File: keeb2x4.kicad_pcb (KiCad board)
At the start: 2 copper layers, 100.6 x 39.9 mm, 36 parts, among them J1 USB_mini_micro_B, K1 KEYSW, K2 KEYSW, K3 KEYSW, K4 KEYSW, K5 KEYSW, K6 KEYSW, K7 KEYSW, K8 KEYSW, SW1 SW_PUSH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

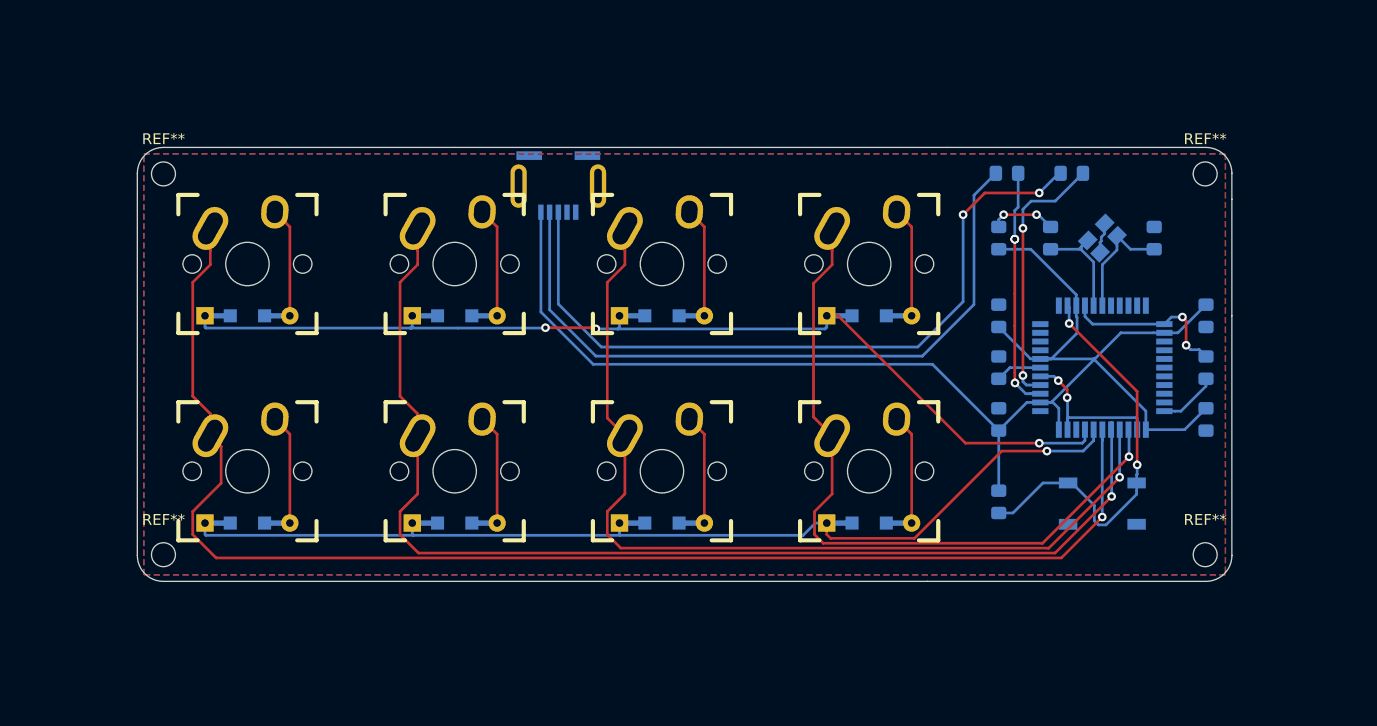
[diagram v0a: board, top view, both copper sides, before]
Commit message: Updated pcb dimensions
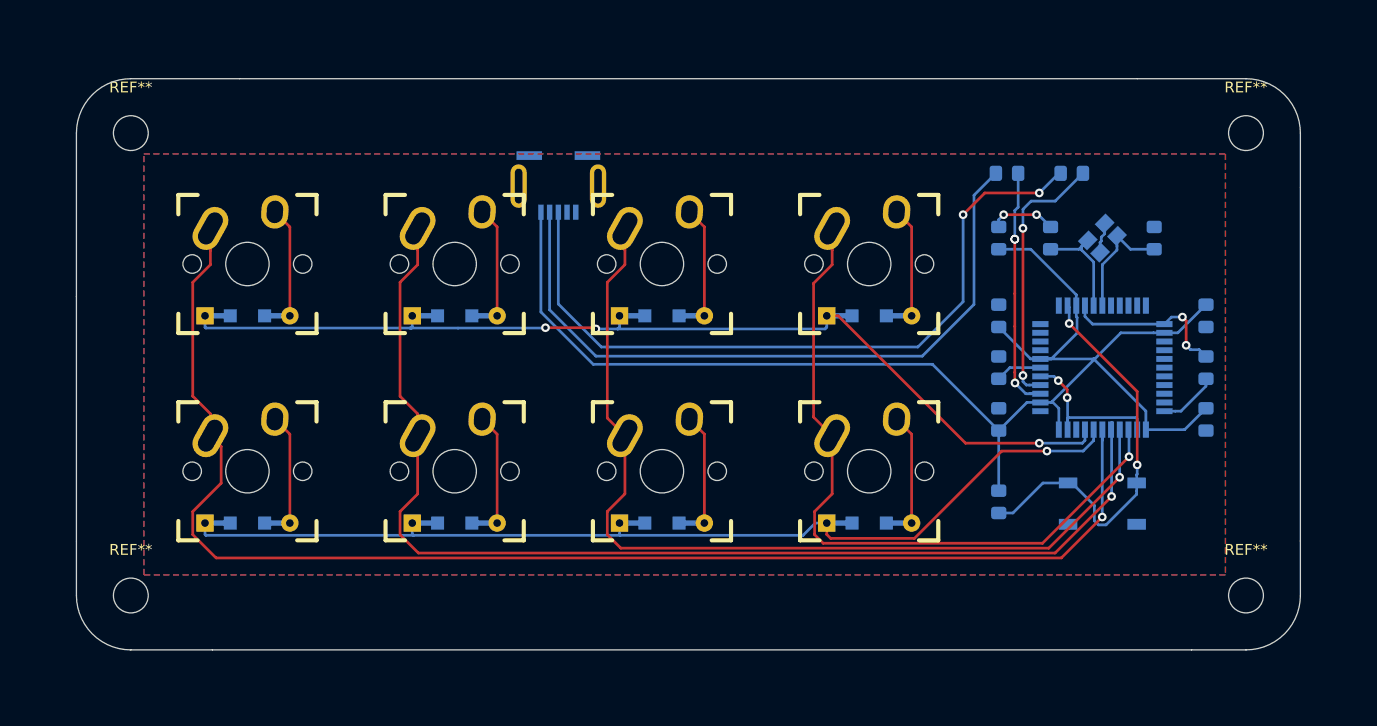
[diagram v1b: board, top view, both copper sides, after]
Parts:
- removed the REF** at (28.0, 86.2)
- removed the REF** at (123.8, 86.2)
- removed the REF** at (123.8, 51.2)
- removed the REF** at (28.0, 51.2)
- added REF**: M3_4, MountingHole:MountingHole_3.2mm_M3, F.Cu at (127.5, 90.0)
- added REF**: M3_3, MountingHole:MountingHole_3.2mm_M3, F.Cu at (25.0, 90.0)
- added REF**: M3_2, MountingHole:MountingHole_3.2mm_M3, F.Cu at (127.5, 47.5)
- added REF**: M3_1, MountingHole:MountingHole_3.2mm_M3, F.Cu at (25.0, 47.5)
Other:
- board size 100.6 x 39.9 mm -> 112.5 x 52.5 mm
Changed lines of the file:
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@@
   (general
     (thickness 1.6)
-    (drawings 14)
+    (drawings 16)
     (tracks 279)
     (zones 0)
@@
     (add_net VCC)
   )
-  (module MountingHole:MountingHole_2.2mm_M2 (layer F.Cu)
-    (at 28 86.25)
-    (descr "Mounting Hole 2.2mm, no annular, M2")
-    (tags "mounting hole 2.2mm no annular m2")
+  (module MountingHole:MountingHole_3.2mm_M3 (layer F.Cu)
+    (at 127.5 90)
+    (descr "Mounting Hole 3.2mm, no annular, M3")
+    (tags "mounting hole 3.2mm no annular m3")
     (attr virtual)
-    (fp_text reference REF** (at 0 -3.2) (layer F.SilkS)
+    (fp_text reference REF** (at 0 -4.2) (layer F.SilkS)
       (effects (font (size 1 1) (thickness 0.15)))
     )
-    (fp_text value M3 (at 0 3.2) (layer F.Fab)
+    (fp_text value M3_4 (at 0 4.2) (layer F.Fab)
       (effects (font (size 1 1) (thickness 0.15)))
     )
-    (fp_circle (center 0 0) (end 2.45 0) (layer F.CrtYd) (width 0.05))
-    (fp_circle (center 0 0) (end 2.2 0) (layer Cmts.User) (width 0.15))
+    (fp_circle (center 0 0) (end 3.45 0) (layer F.CrtYd) (width 0.05))
+    (fp_circle (center 0 0) (end 3.2 0) (layer Cmts.User) (width 0.15))
     (fp_text user %R (at 0.3 0) (layer F.Fab)
       (effects (font (size 1 1) (thickness 0.15)))
     )
-    (pad 1 np_thru_hole circle (at 0 0) (size 2.2 2.2) (drill 2.2) (layers *.Cu *.Mask))
-  )
-  (module MountingHole:MountingHole_2.2mm_M2 (layer F.Cu)
-    (at 123.75 86.25)
-    (descr "Mounting Hole 2.2mm, no annular, M2")
-    (tags "mounting hole 2.2mm no annular m2")
+    (pad 1 np_thru_hole circle (at 0 0) (size 3.2 3.2) (drill 3.2) (layers *.Cu *.Mask))
+  )
+  (module MountingHole:MountingHole_3.2mm_M3 (layer F.Cu)
+    (at 25 90)
+    (descr "Mounting Hole 3.2mm, no annular, M3")
+    (tags "mounting hole 3.2mm no annular m3")
     (attr virtual)
-    (fp_text reference REF** (at 0 -3.2) (layer F.SilkS)
+    (fp_text reference REF** (at 0 -4.2) (layer F.SilkS)
       (effects (font (size 1 1) (thickness 0.15)))
     )
-    (fp_text value M4 (at 0 3.2) (layer F.Fab)
+    (fp_text value M3_3 (at 0 4.2) (layer F.Fab)
       (effects (font (size 1 1) (thickness 0.15)))
     )
-    (fp_circle (center 0 0) (end 2.45 0) (layer F.CrtYd) (width 0.05))
-    (fp_circle (center 0 0) (end 2.2 0) (layer Cmts.User) (width 0.15))
+    (fp_circle (center 0 0) (end 3.45 0) (layer F.CrtYd) (width 0.05))
+    (fp_circle (center 0 0) (end 3.2 0) (layer Cmts.User) (width 0.15))
     (fp_text user %R (at 0.3 0) (layer F.Fab)
       (effects (font (size 1 1) (thickness 0.15)))
     )
-    (pad 1 np_thru_hole circle (at 0 0) (size 2.2 2.2) (drill 2.2) (layers *.Cu *.Mask))
-  )
-  (module MountingHole:MountingHole_2.2mm_M2 (layer F.Cu)
-    (at 123.75 51.25)
-    (descr "Mounting Hole 2.2mm, no annular, M2")
-    (tags "mounting hole 2.2mm no annular m2")
+    (pad 1 np_thru_hole circle (at 0 0) (size 3.2 3.2) (drill 3.2) (layers *.Cu *.Mask))
+  )
+  (module MountingHole:MountingHole_3.2mm_M3 (layer F.Cu)
+    (at 127.5 47.5)
+    (descr "Mounting Hole 3.2mm, no annular, M3")
+    (tags "mounting hole 3.2mm no annular m3")
     (attr virtual)
-    (fp_text reference REF** (at 0 -3.2) (layer F.SilkS)
+    (fp_text reference REF** (at 0 -4.2) (layer F.SilkS)
       (effects (font (size 1 1) (thickness 0.15)))
     )
-    (fp_text value M2 (at 0 3.2) (layer F.Fab)
+    (fp_text value M3_2 (at 0 4.2) (layer F.Fab)
       (effects (font (size 1 1) (thickness 0.15)))
     )
-    (fp_circle (center 0 0) (end 2.45 0) (layer F.CrtYd) (width 0.05))
-    (fp_circle (center 0 0) (end 2.2 0) (layer Cmts.User) (width 0.15))
+    (fp_circle (center 0 0) (end 3.45 0) (layer F.CrtYd) (width 0.05))
+    (fp_circle (center 0 0) (end 3.2 0) (layer Cmts.User) (width 0.15))
     (fp_text user %R (at 0.3 0) (layer F.Fab)
       (effects (font (size 1 1) (thickness 0.15)))
     )
-    (pad 1 np_thru_hole circle (at 0 0) (size 2.2 2.2) (drill 2.2) (layers *.Cu *.Mask))
-  )
-  (module MountingHole:MountingHole_2.2mm_M2 (layer F.Cu)
-    (at 28 51.25)
-    (descr "Mounting Hole 2.2mm, no annular, M2")
-    (tags "mounting hole 2.2mm no annular m2")
+    (pad 1 np_thru_hole circle (at 0 0) (size 3.2 3.2) (drill 3.2) (layers *.Cu *.Mask))
+  )
+  (module MountingHole:MountingHole_3.2mm_M3 (layer F.Cu)
+    (at 25 47.5)
+    (descr "Mounting Hole 3.2mm, no annular, M3")
+    (tags "mounting hole 3.2mm no annular m3")
     (attr virtual)
-    (fp_text reference REF** (at 0 -3.2) (layer F.SilkS)
+    (fp_text reference REF** (at 0 -4.2) (layer F.SilkS)
       (effects (font (size 1 1) (thickness 0.15)))
     )
-    (fp_text value M1 (at 0 3.2) (layer F.Fab)
+    (fp_text value M3_1 (at 0 4.2) (layer F.Fab)
       (effects (font (size 1 1) (thickness 0.15)))
     )
-    (fp_circle (center 0 0) (end 2.45 0) (layer F.CrtYd) (width 0.05))
-    (fp_circle (center 0 0) (end 2.2 0) (layer Cmts.User) (width 0.15))
+    (fp_circle (center 0 0) (end 3.45 0) (layer F.CrtYd) (width 0.05))
+    (fp_circle (center 0 0) (end 3.2 0) (layer Cmts.User) (width 0.15))
     (fp_text user %R (at 0.3 0) (layer F.Fab)
       (effects (font (size 1 1) (thickness 0.15)))
     )
-    (pad 1 np_thru_hole circle (at 0 0) (size 2.2 2.2) (drill 2.2) (layers *.Cu *.Mask))
+    (pad 1 np_thru_hole circle (at 0 0) (size 3.2 3.2) (drill 3.2) (layers *.Cu *.Mask))
   )
   (module Capacitor_SMD:C_0805_2012Metric_Pad1.15x1.40mm_HandSolder (layer B.Cu)
@@
     )
   )
-  (gr_line (start 27.979711 88.701637) (end 98.226645 88.701637) (layer Edge.Cuts) (width 0.05))
-  (gr_arc (start 27.979711 86.320385) (end 25.598459 86.320385) (angle -90) (layer Edge.Cuts) (width 0.05))
-  (gr_line (start 123.825104 88.701637) (end 98.226645 88.701637) (layer Edge.Cuts) (width 0.05))
-  (gr_line (start 27.979711 48.815666) (end 54.768796 48.815666) (layer Edge.Cuts) (width 0.05))
-  (gr_line (start 25.598459 86.320385) (end 25.598459 51.196918) (layer Edge.Cuts) (width 0.05))
-  (gr_arc (start 27.979711 51.196918) (end 27.979711 48.815666) (angle -90) (layer Edge.Cuts) (width 0.05))
-  (gr_arc (start 123.825104 86.320385) (end 123.825104 88.701637) (angle -90) (layer Edge.Cuts) (width 0.05))
-  (gr_line (start 126.206356 64.293804) (end 126.206356 86.320385) (layer Edge.Cuts) (width 0.05))
-  (gr_line (start 123.825104 48.815666) (end 119.0626 48.815666) (layer Edge.Cuts) (width 0.05))
-  (gr_line (start 126.206356 53.57817) (end 126.206356 51.196918) (layer Edge.Cuts) (width 0.05))
-  (gr_arc (start 123.825104 51.196918) (end 126.206356 51.196918) (angle -90) (layer Edge.Cuts) (width 0.05))
-  (gr_line (start 126.206356 64.293804) (end 126.206356 53.57817) (layer Edge.Cuts) (width 0.05))
-  (gr_line (start 100.012584 48.815666) (end 119.0626 48.815666) (layer Edge.Cuts) (width 0.05))
-  (gr_line (start 54.768796 48.815666) (end 100.012584 48.815666) (layer Edge.Cuts) (width 0.05))
+  (gr_line (start 132.5 47.5) (end 132.5 52.5) (layer Edge.Cuts) (width 0.05))
+  (gr_line (start 117.5 42.5) (end 127.5 42.5) (layer Edge.Cuts) (width 0.05))
+  (gr_line (start 25 42.5) (end 35 42.5) (layer Edge.Cuts) (width 0.05))
+  (gr_line (start 20 62.5) (end 20 47.5) (layer Edge.Cuts) (width 0.05))
+  (gr_line (start 20 90) (end 20 85) (layer Edge.Cuts) (width 0.05))
+  (gr_line (start 32.5 95) (end 25 95) (layer Edge.Cuts) (width 0.05))
+  (gr_line (start 127.5 95) (end 122.5 95) (layer Edge.Cuts) (width 0.05))
+  (gr_line (start 132.5 90) (end 132.5 85) (layer Edge.Cuts) (width 0.05))
+  (gr_arc (start 127.5 90) (end 127.5 95) (angle -90) (layer Edge.Cuts) (width 0.05))
+  (gr_arc (start 127.5 47.5) (end 132.5 47.5) (angle -90) (layer Edge.Cuts) (width 0.05))
+  (gr_arc (start 25 47.5) (end 25 42.5) (angle -90) (layer Edge.Cuts) (width 0.05))
+  (gr_arc (start 25 90) (end 20 90) (angle -90) (layer Edge.Cuts) (width 0.05))
+  (gr_line (start 20 62.5) (end 20 85) (layer Edge.Cuts) (width 0.05))
+  (gr_line (start 132.5 52.5) (end 132.5 85) (layer Edge.Cuts) (width 0.05))
+  (gr_line (start 35 42.5) (end 117.5 42.5) (layer Edge.Cuts) (width 0.05))
+  (gr_line (start 32.5 95) (end 122.5 95) (layer Edge.Cuts) (width 0.05))
   (segment (start 114.200746 57.066411) (end 114.512132 56.755025) (width 0.25) (layer B.Cu) (net 1))
   (segment (start 114.512132 56.755025) (end 114.512132 55.806497) (width 0.25) (layer B.Cu) (net 1))

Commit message: added case files
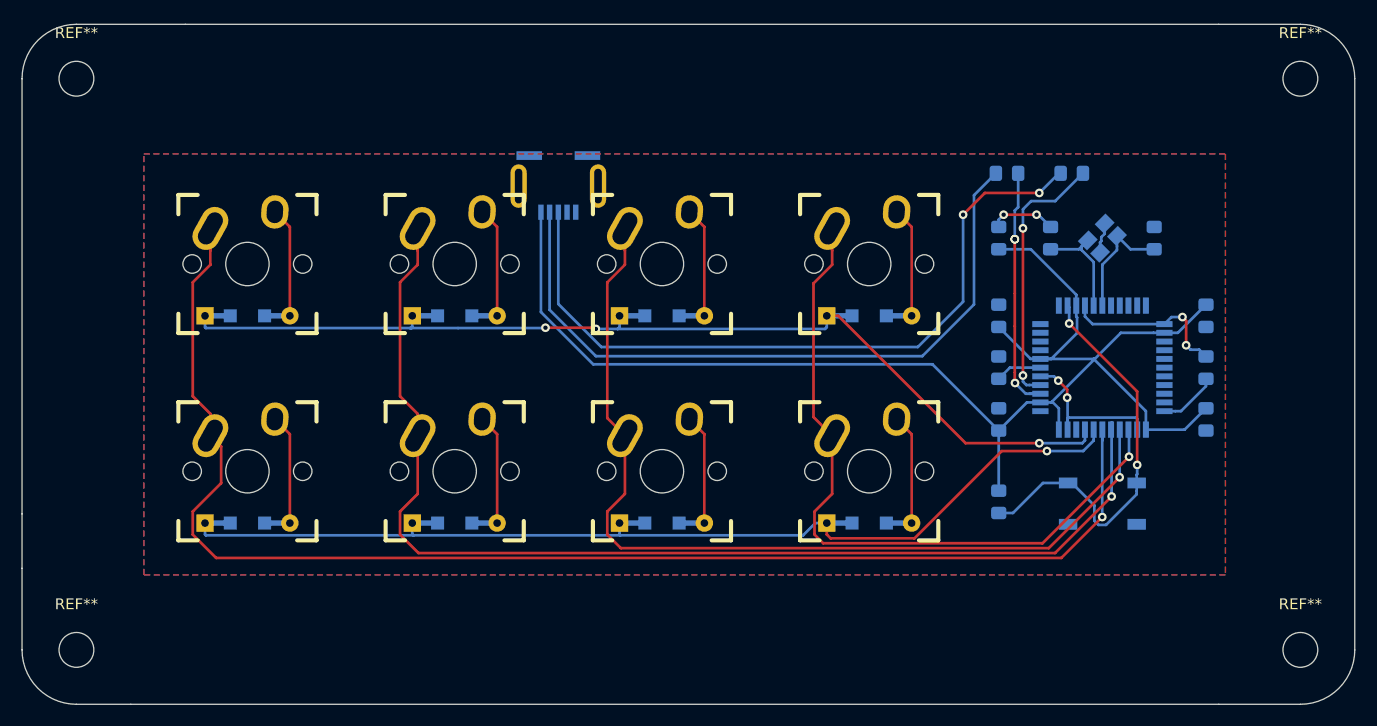
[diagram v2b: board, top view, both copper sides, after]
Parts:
- moved REF** 7.07 mm to (132.5, 95.0)
- moved REF** 7.07 mm to (20.0, 95.0)
- moved REF** 7.07 mm to (132.5, 42.5)
- moved REF** 7.07 mm to (20.0, 42.5)
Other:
- board size 112.5 x 52.5 mm -> 122.5 x 62.5 mm
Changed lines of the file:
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@@
   (general
     (thickness 1.6)
-    (drawings 16)
+    (drawings 14)
     (tracks 279)
     (zones 0)
@@
     (pcbplotparams
       (layerselection 0x010fc_ffffffff)
-      (usegerberextensions false)
+      (usegerberextensions true)
       (usegerberattributes false)
       (usegerberadvancedattributes false)
@@
       (outputformat 1)
       (mirror false)
-      (drillshape 1)
+      (drillshape 0)
       (scaleselection 1)
-      (outputdirectory ""))
+      (outputdirectory "gerber/"))
   )
   (net 0 "")
@@
   )
   (module MountingHole:MountingHole_3.2mm_M3 (layer F.Cu)
-    (at 127.5 90)
+    (at 132.5 95)
     (descr "Mounting Hole 3.2mm, no annular, M3")
     (tags "mounting hole 3.2mm no annular m3")
@@
   )
   (module MountingHole:MountingHole_3.2mm_M3 (layer F.Cu)
-    (at 25 90)
+    (at 20 95)
     (descr "Mounting Hole 3.2mm, no annular, M3")
     (tags "mounting hole 3.2mm no annular m3")
@@
   )
   (module MountingHole:MountingHole_3.2mm_M3 (layer F.Cu)
-    (at 127.5 47.5)
+    (at 132.5 42.5)
     (descr "Mounting Hole 3.2mm, no annular, M3")
     (tags "mounting hole 3.2mm no annular m3")
@@
   )
   (module MountingHole:MountingHole_3.2mm_M3 (layer F.Cu)
-    (at 25 47.5)
+    (at 20 42.5)
     (descr "Mounting Hole 3.2mm, no annular, M3")
     (tags "mounting hole 3.2mm no annular m3")
@@
     )
   )
-  (gr_line (start 132.5 47.5) (end 132.5 52.5) (layer Edge.Cuts) (width 0.05))
-  (gr_line (start 117.5 42.5) (end 127.5 42.5) (layer Edge.Cuts) (width 0.05))
-  (gr_line (start 25 42.5) (end 35 42.5) (layer Edge.Cuts) (width 0.05))
-  (gr_line (start 20 62.5) (end 20 47.5) (layer Edge.Cuts) (width 0.05))
-  (gr_line (start 20 90) (end 20 85) (layer Edge.Cuts) (width 0.05))
-  (gr_line (start 32.5 95) (end 25 95) (layer Edge.Cuts) (width 0.05))
-  (gr_line (start 127.5 95) (end 122.5 95) (layer Edge.Cuts) (width 0.05))
-  (gr_line (start 132.5 90) (end 132.5 85) (layer Edge.Cuts) (width 0.05))
-  (gr_arc (start 127.5 90) (end 127.5 95) (angle -90) (layer Edge.Cuts) (width 0.05))
-  (gr_arc (start 127.5 47.5) (end 132.5 47.5) (angle -90) (layer Edge.Cuts) (width 0.05))
-  (gr_arc (start 25 47.5) (end 25 42.5) (angle -90) (layer Edge.Cuts) (width 0.05))
-  (gr_arc (start 25 90) (end 20 90) (angle -90) (layer Edge.Cuts) (width 0.05))
-  (gr_line (start 20 62.5) (end 20 85) (layer Edge.Cuts) (width 0.05))
-  (gr_line (start 132.5 52.5) (end 132.5 85) (layer Edge.Cuts) (width 0.05))
-  (gr_line (start 35 42.5) (end 117.5 42.5) (layer Edge.Cuts) (width 0.05))
-  (gr_line (start 32.5 95) (end 122.5 95) (layer Edge.Cuts) (width 0.05))
+  (gr_arc (start 132.5 95) (end 132.5 100) (angle -90) (layer Edge.Cuts) (width 0.05))
+  (gr_line (start 125 100) (end 132.5 100) (layer Edge.Cuts) (width 0.05))
+  (gr_line (start 137.5 42.5) (end 137.5 95) (layer Edge.Cuts) (width 0.05))
+  (gr_arc (start 132.5 42.5) (end 137.5 42.5) (angle -90) (layer Edge.Cuts) (width 0.05))
+  (gr_line (start 125 37.5) (end 132.5 37.5) (layer Edge.Cuts) (width 0.05))
+  (gr_arc (start 20 42.5) (end 20 37.5) (angle -90) (layer Edge.Cuts) (width 0.05))
+  (gr_line (start 30 37.5) (end 20 37.5) (layer Edge.Cuts) (width 0.05))
+  (gr_line (start 15 82.5) (end 15 42.5) (layer Edge.Cuts) (width 0.05))
+  (gr_line (start 30 37.5) (end 125 37.5) (layer Edge.Cuts) (width 0.05))
+  (gr_line (start 15 95) (end 15 87.5) (layer Edge.Cuts) (width 0.05))
+  (gr_line (start 20 100) (end 25 100) (layer Edge.Cuts) (width 0.05))
+  (gr_arc (start 20 95) (end 15 95) (angle -90) (layer Edge.Cuts) (width 0.05))
+  (gr_line (start 25 100) (end 125 100) (layer Edge.Cuts) (width 0.05))
+  (gr_line (start 15 82.5) (end 15 87.5) (layer Edge.Cuts) (width 0.05))
   (segment (start 114.200746 57.066411) (end 114.512132 56.755025) (width 0.25) (layer B.Cu) (net 1))
   (segment (start 114.512132 56.755025) (end 114.512132 55.806497) (width 0.25) (layer B.Cu) (net 1))
